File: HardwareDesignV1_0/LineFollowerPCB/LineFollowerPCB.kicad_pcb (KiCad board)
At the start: 2 copper layers, 152 x 100 mm, 11 parts, among them J1 B2B-XH-A, J2 B4B-XH-A, J3 Conn_01x04, M1 Motor_DC, M2 Motor_DC, U1 Black Pill v2, U2 DRV8833, U3 AMS1117-3.3, U4 SX1308

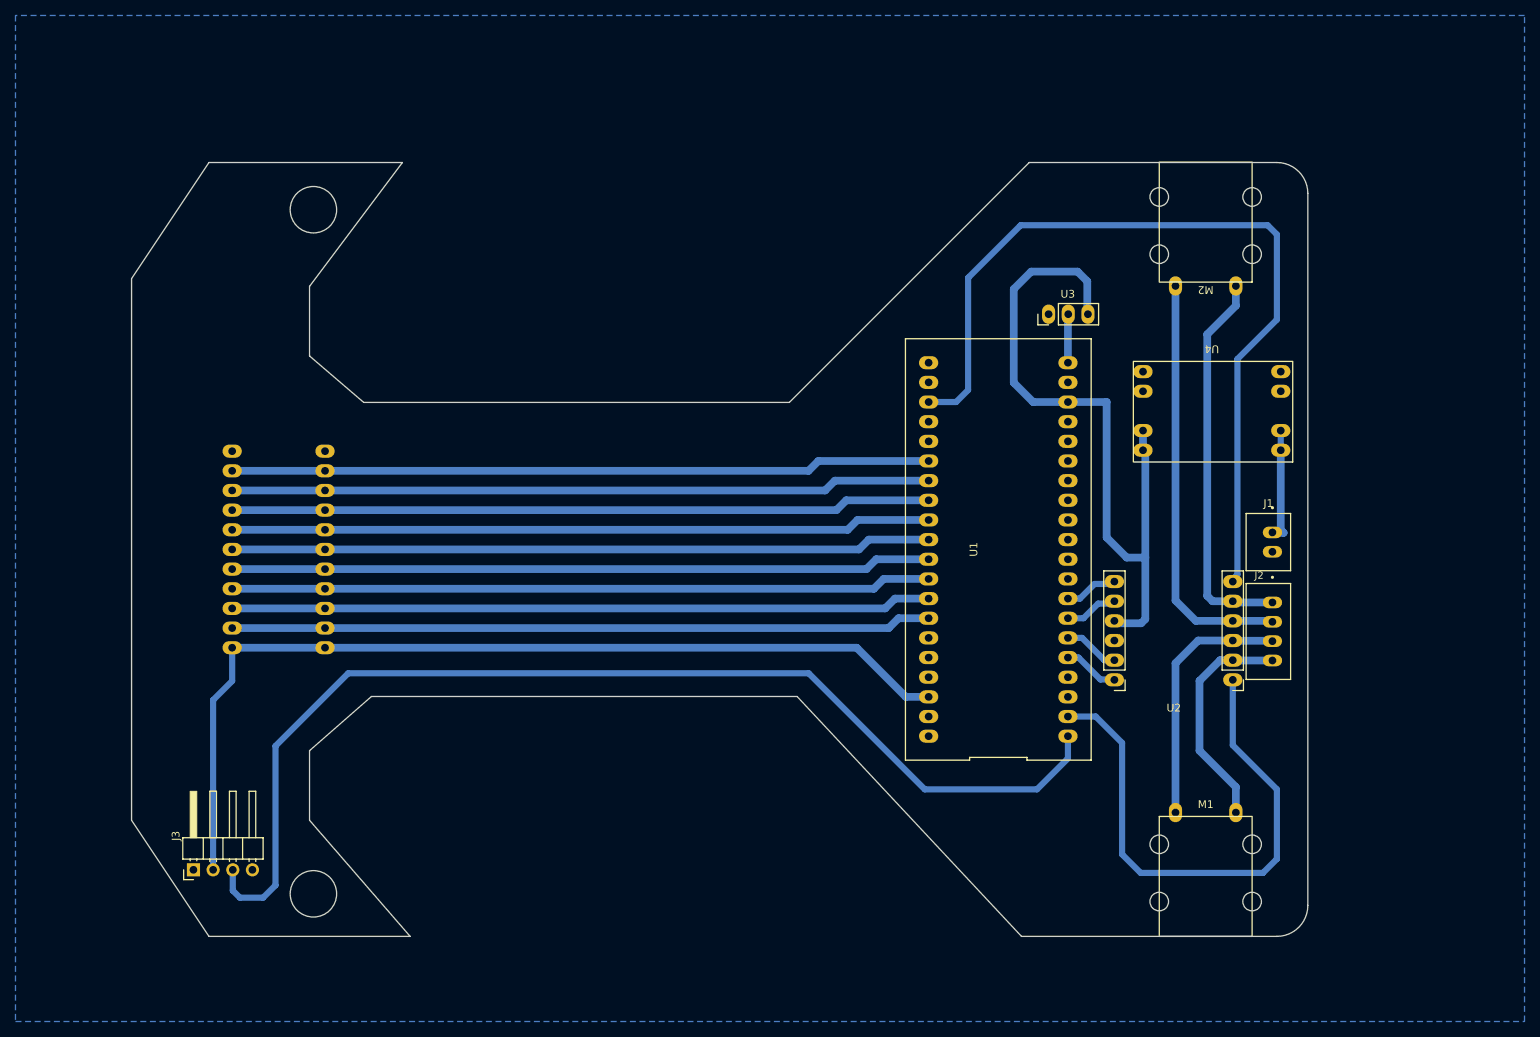
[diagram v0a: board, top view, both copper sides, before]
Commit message: - Add Shunt bridge for power switching ON-OFF - Edit DC motor footprint library - Add solder jumber for select between QTR / Cytron sensors
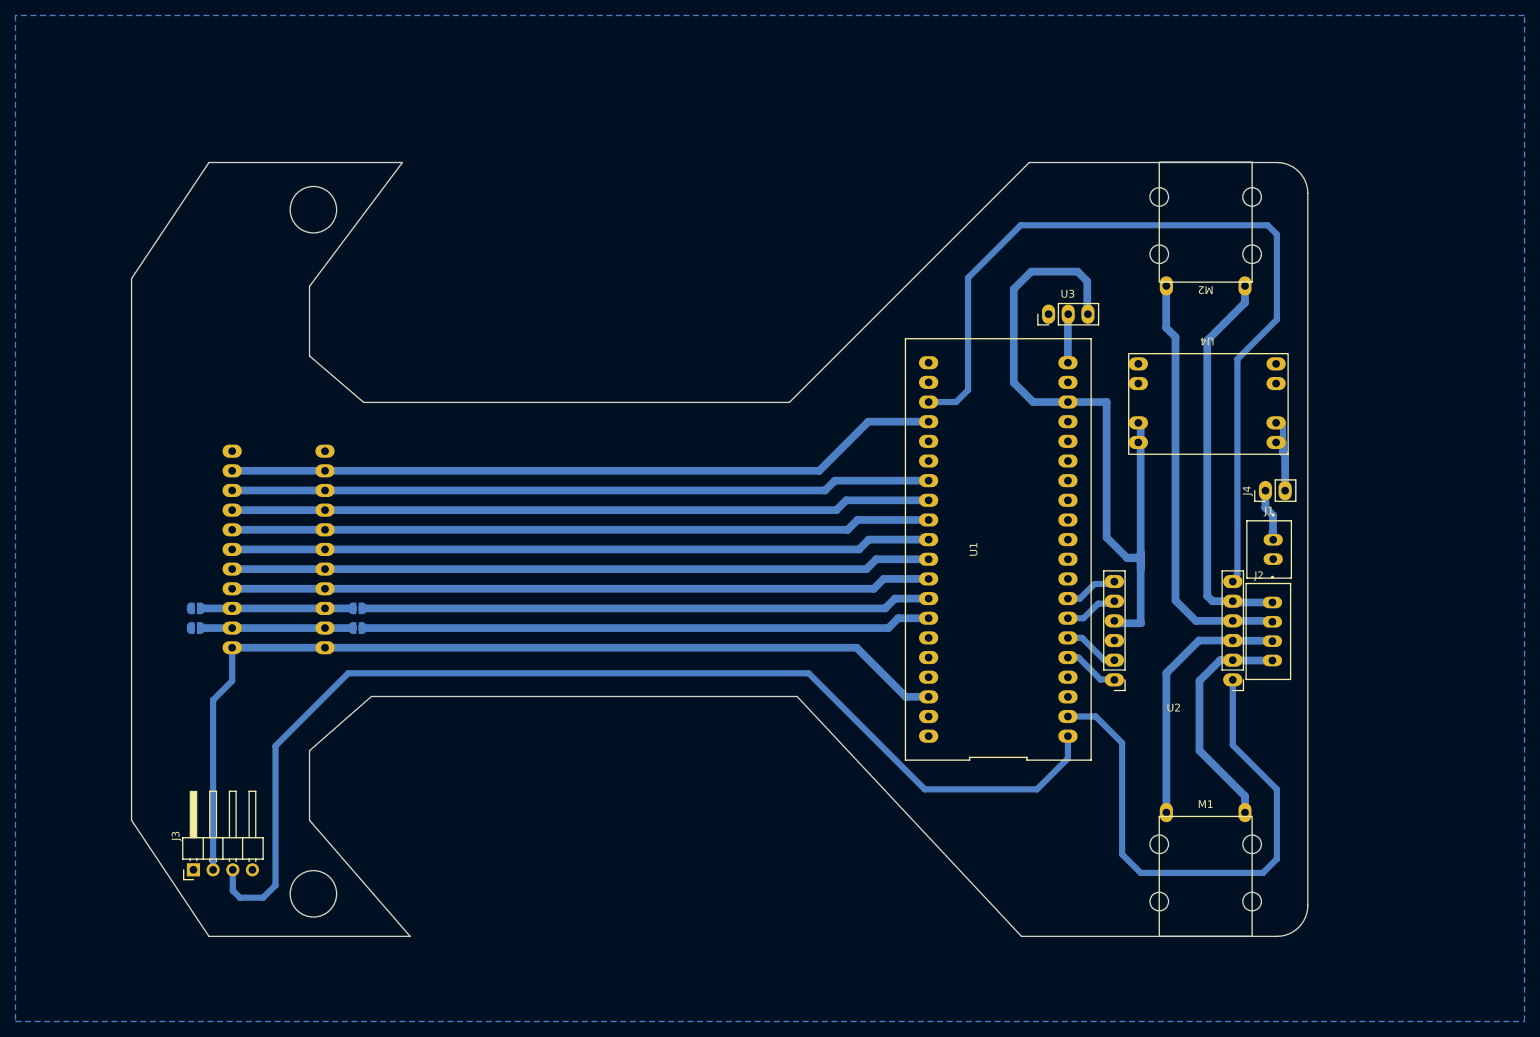
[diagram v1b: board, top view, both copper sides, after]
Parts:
- added J4: Conn_01x02_Socket, Connector_PinHeader_2.54mm:PinHeader_1x02_P2.54mm_Vertical, F.Cu at (216.5, 81.4)
- added JP1: SolderJumper_3_Open, Jumper:SolderJumper-2_P1.3mm_Open_RoundedPad1.0x1.5mm, B.Cu at (99.2, 99.2)
- added JP2: SolderJumper_3_Open, Jumper:SolderJumper-2_P1.3mm_Open_RoundedPad1.0x1.5mm, B.Cu at (78.3, 99.2)
- added JP3: SolderJumper_3_Open, Jumper:SolderJumper-2_P1.3mm_Open_RoundedPad1.0x1.5mm, B.Cu at (99.2, 96.6)
- added JP4: SolderJumper_3_Open, Jumper:SolderJumper-2_P1.3mm_Open_RoundedPad1.0x1.5mm, B.Cu at (78.3, 96.6)
- moved U4 1.17 mm to (209.0, 70.1)
- moved J1 0.96 mm to (217.0, 89.0)
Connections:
- U1 pad 24: unconnected-(U1-PC15-Pad24) -> IR_SG
- U1 pad 26: IR_SG -> unconnected-(U1-PA0-Pad26)
- U4 pad 1: 3.7V -> VIN
- U5 pad 10: D8 -> /SEL1
- U5 pad 9: D7 -> /SEL2
- U6 pad 10: D8 -> /SEL1
- U6 pad 9: D7 -> /SEL2
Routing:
- net /SEL2: track 0.00 -> 19.6 mm
- net /SEL1: track 0.00 -> 19.6 mm
- net D7: track 90.5 -> 73.5 mm
- net D8: track 90.5 -> 73.7 mm
- net VIN: track 0.00 -> 8.87 mm
- net 3.7V: track 14.1 -> 5.85 mm
- net 5.5V: track 92.8 -> 96.7 mm
- net IR_SG: track 90.5 -> 92.6 mm
- net OUT3: track 54.8 -> 55.3 mm
